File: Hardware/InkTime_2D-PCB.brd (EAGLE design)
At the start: 46 x 35 mm, 105 parts, among them IC1 BQ25180YBGR, IC2 DRV2605YZFR, IC3 BMA421, IC9 RT6160AWSC, J1 503480-2400, J2 TC2030-IDC, J4 KH-TYPE-C-16P, Q1 20V/4.2A/52mΩ/1.4W, Q3 SI1308EDL-T1-GE3, U1 NRF52840 _QF, U3 MAX17048G+T10, X1 32MHz, X2 32.768KHz

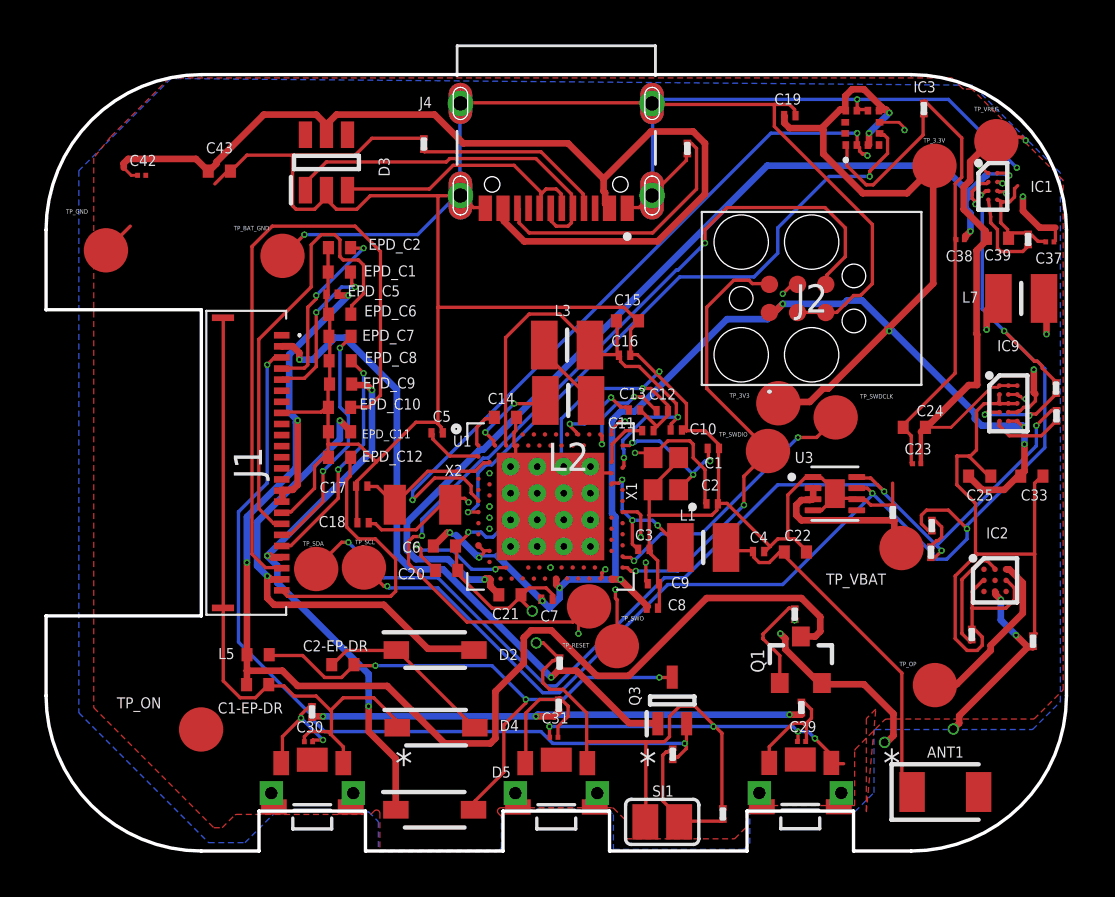
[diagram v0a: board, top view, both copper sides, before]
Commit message: Added Via Stiching to GND planes
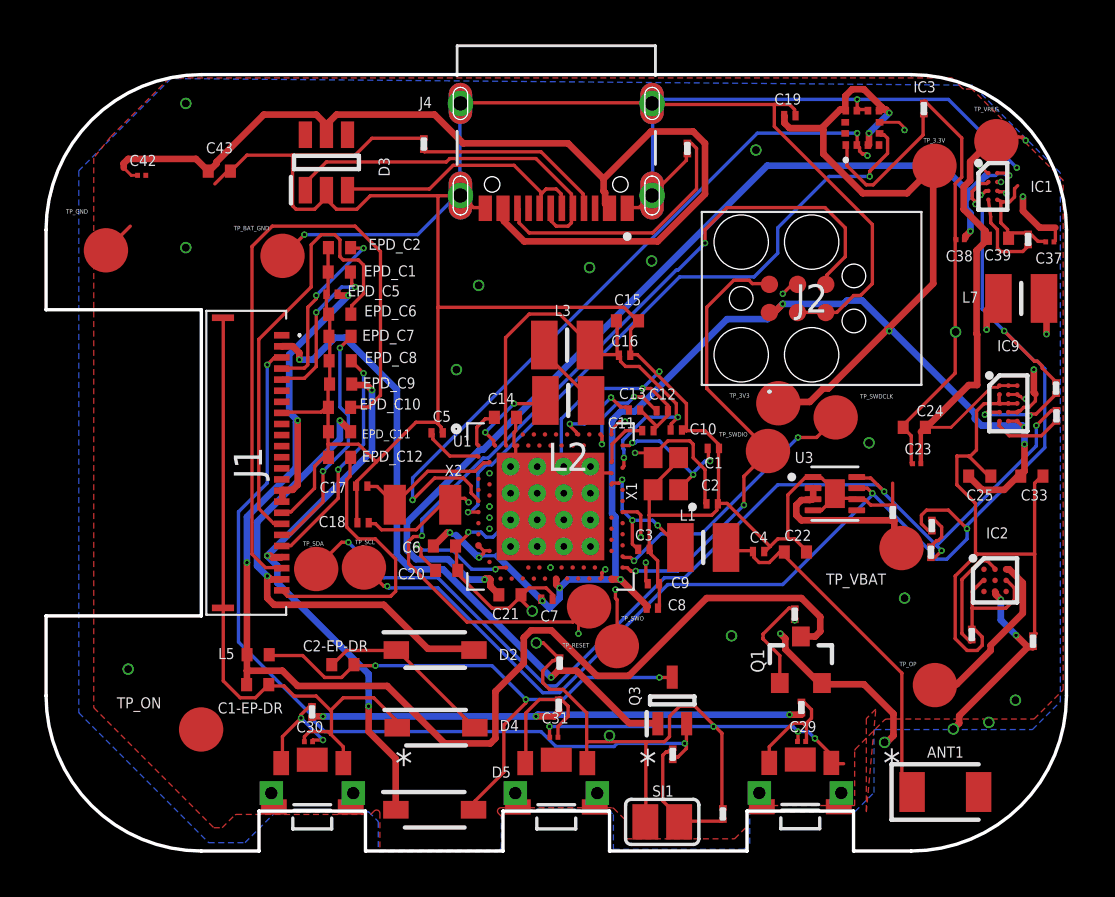
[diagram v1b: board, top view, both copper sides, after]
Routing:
- net GND: vias 12 -> 27
